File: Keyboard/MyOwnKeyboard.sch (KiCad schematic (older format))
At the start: 465 parts, among them J1 Mini-DIN-6, Q1 RFD14N05L, SW1 SW_SPST, SW10 SW_SPST, SW100 SW_SPST, SW101 SW_SPST, SW102 SW_SPST, SW103 SW_SPST, SW104 SW_SPST, SW105 SW_SPST, SW106 SW_SPST, SW107 SW_SPST, SW108 SW_SPST, SW109 SW_SPST, SW11 SW_SPST, SW110 SW_SPST, SW111 SW_SPST, SW112 SW_SPST, SW113 SW_SPST, SW114 SW_SPST, SW12 SW_SPST, SW13 SW_SPST, SW14 SW_SPST, SW15 SW_SPST, SW16 SW_SPST, SW17 SW_SPST, SW18 SW_SPST, SW19 SW_SPST, SW2 SW_SPST, SW20 SW_SPST, SW21 SW_SPST, SW22 SW_SPST, SW23 SW_SPST, SW24 SW_SPST, SW25 SW_SPST, SW26 SW_SPST, SW27 SW_SPST, SW28 SW_SPST, SW29 SW_SPST, SW3 SW_SPST, SW30 SW_SPST, SW31 SW_SPST, SW32 SW_SPST, SW33 SW_SPST, SW34 SW_SPST, SW35 SW_SPST, SW36 SW_SPST, SW37 SW_SPST, SW38 SW_SPST, SW39 SW_SPST, SW4 SW_SPST, SW40 SW_SPST, SW41 SW_SPST, SW42 SW_SPST, SW43 SW_SPST, SW44 SW_SPST, SW45 SW_SPST, SW46 SW_SPST, SW47 SW_SPST, SW48 SW_SPST, SW49 SW_SPST, SW5 SW_SPST, SW50 SW_SPST, SW51 SW_SPST, SW52 SW_SPST, SW53 SW_SPST, SW54 SW_SPST, SW55 SW_SPST, SW56 SW_SPST, SW57 SW_SPST, SW58 SW_SPST, SW59 SW_SPST, SW6 SW_SPST, SW60 SW_SPST, SW61 SW_SPST, SW62 SW_SPST, SW63 SW_SPST, SW64 SW_SPST, SW65 SW_SPST, SW66 SW_SPST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

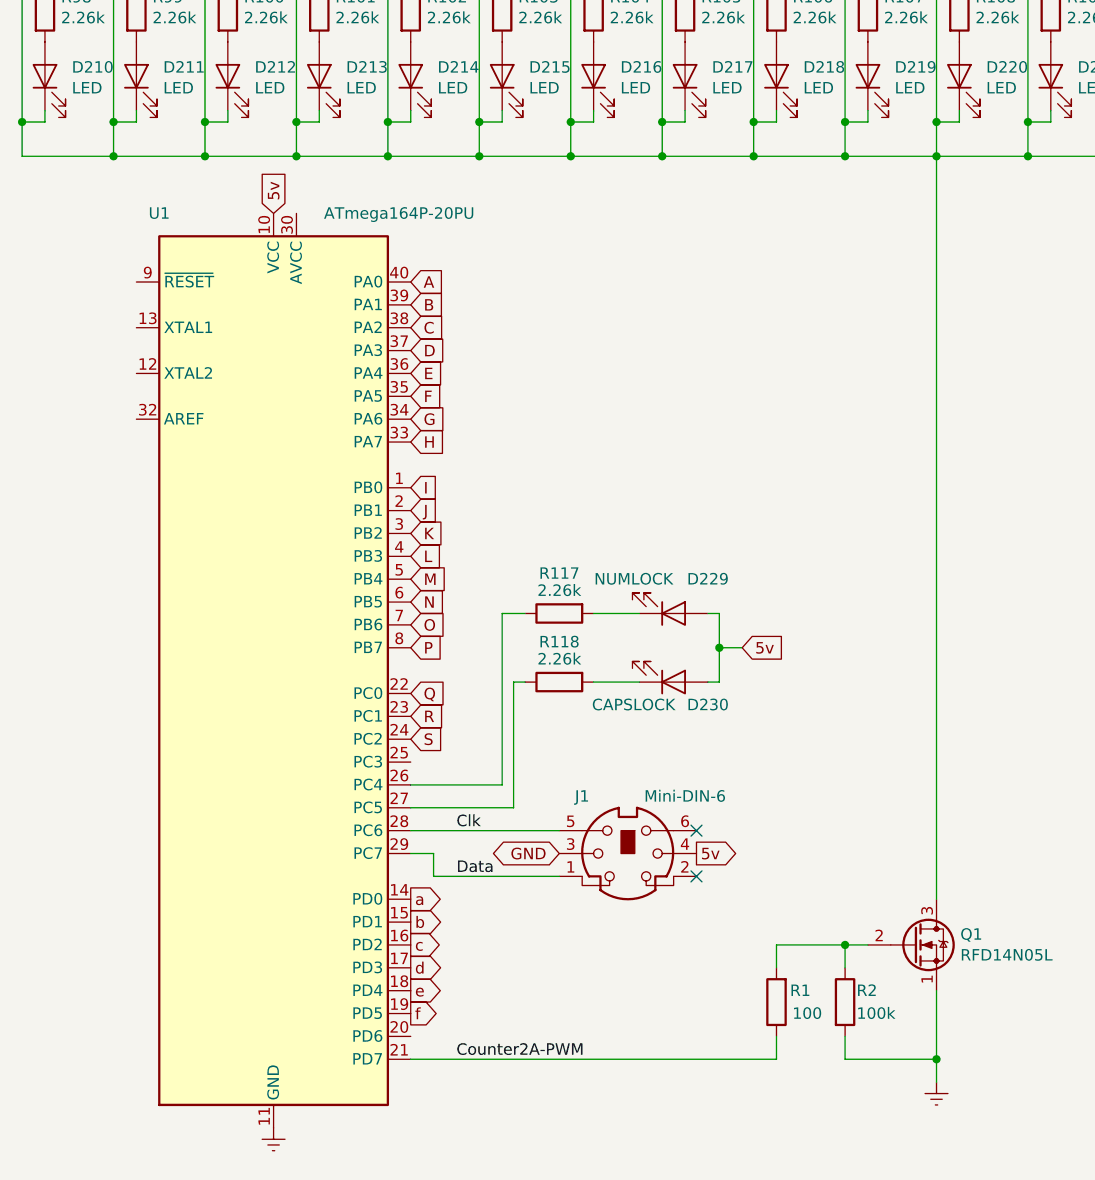
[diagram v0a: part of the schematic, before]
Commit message: Update keyboard to match changes to keypad
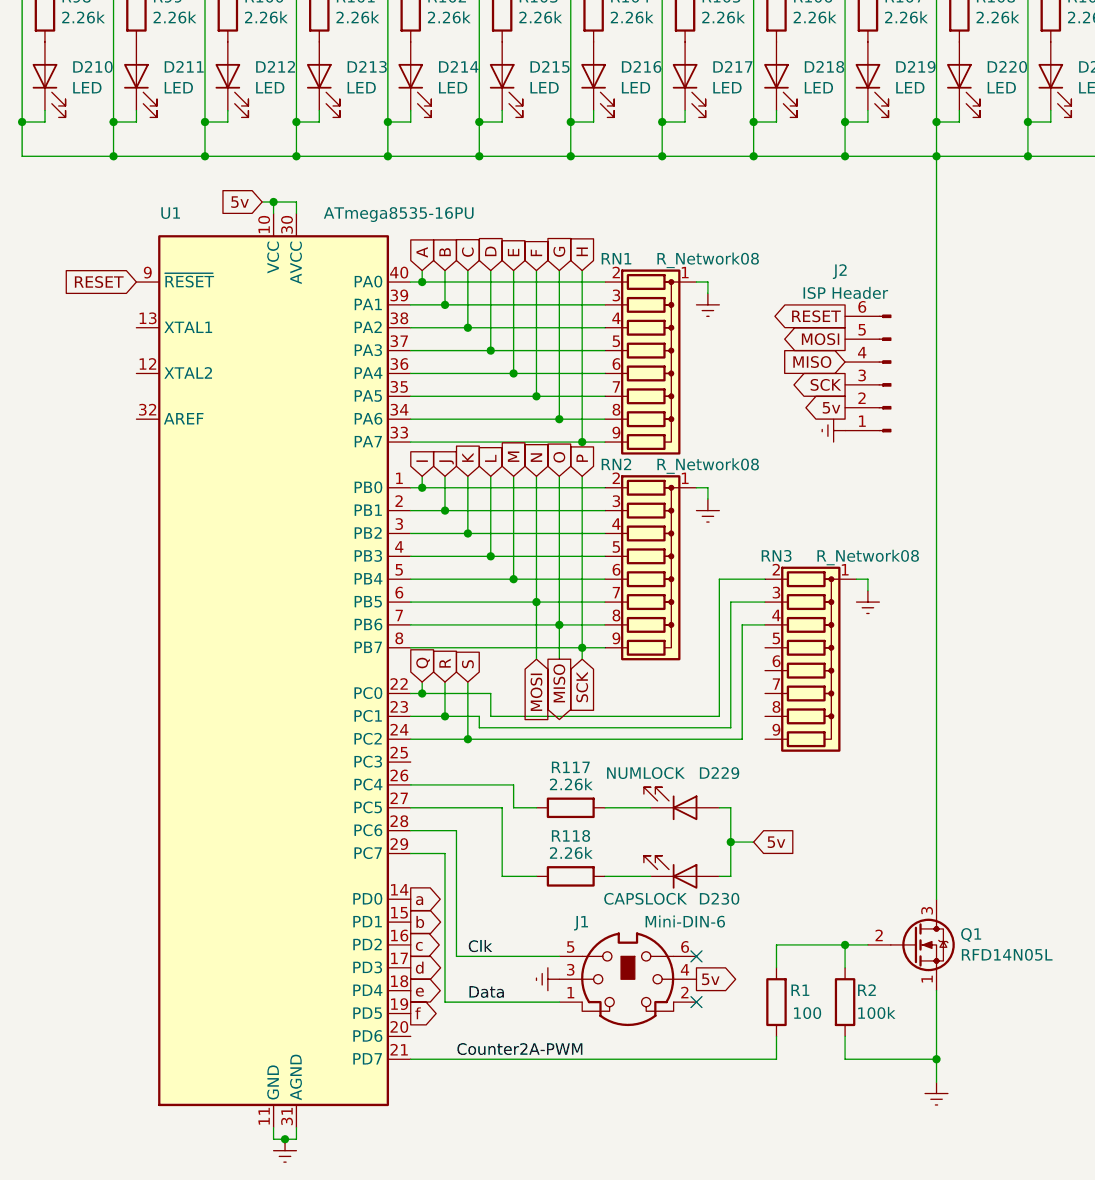
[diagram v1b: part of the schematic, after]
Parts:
- removed U1: ATmega164P-20PU, Package_DIP:DIP-40_W15.24mm, symbol MyOwnKeyboard-rescue:ATmega164P-20PU-MCU_Microchip_ATmega-MyOwnKeyboard-rescue
- added J2: ISP Header, Connector_PinHeader_2.54mm:PinHeader_2x03_P2.54mm_Vertical, symbol Connector:Conn_01x06_Male
- added RN1, RN2, RN3: R_Network08, Resistor_THT:R_Array_SIP9, symbol Device:R_Network08
- added U1: ATmega8535-16PU, Package_DIP:DIP-40_W15.24mm, symbol MCU_Microchip_ATmega:ATmega8535-16PU
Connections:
- net GND is gone; now on net Earth: J1.3
- net 5v: now also J2.2 (Pin_2), U1.10 (VCC), U1.30 (AVCC)
- net A: now also RN1.2 (R1), U1.40 (PA0)
- net B: now also RN1.3 (R2), U1.39 (PA1)
- net C: now also RN1.4 (R3), U1.38 (PA2)
- net Clk: now also U1.28 (PC6)
- net Counter2A-PWM: now also U1.21 (PD7)
- net D: now also RN1.5 (R4), U1.37 (PA3)
- net Data: now also U1.29 (PC7)
- net E: now also RN1.6 (R5), U1.36 (PA4)
- net Earth: now also J2.1 (Pin_1), RN1.1 (common), RN2.1 (common), RN3.1 (common), U1.11 (GND), U1.31 (AGND)
- net F: now also RN1.7 (R6), U1.35 (PA5)
- net G: now also RN1.8 (R7), U1.34 (PA6)
- net H: now also RN1.9 (R8), U1.33 (PA7)
- net I: now also RN2.2 (R1), U1.1 (PB0)
- net J: now also RN2.3 (R2), U1.2 (PB1)
- net K: now also RN2.4 (R3), U1.3 (PB2)
- net L: now also RN2.5 (R4), U1.4 (PB3)
- net M: now also RN2.6 (R5), U1.5 (PB4)
- net P: now also J2.3 (Pin_3), RN2.9 (R8), U1.8 (PB7)
- net Q: now also RN3.2 (R1), U1.22 (PC0)
- net R: now also RN3.3 (R2), U1.23 (PC1)
- net S: now also RN3.4 (R3), U1.24 (PC2)
- net a: now also U1.14 (PD0)
- net b: now also U1.15 (PD1)
- net c: now also U1.16 (PD2)
- net d: now also U1.17 (PD3)
- net e: now also U1.18 (PD4)
- net f: now also U1.19 (PD5)
- net at R117.1: now also U1.26 (PC4)
- net at R118.1: now also U1.27 (PC5)
- net N renamed MOSI
- net MOSI: now also J2.5 (Pin_5), RN2.7 (R6), U1.6 (PB5)
- net O renamed MISO
- net MISO: now also J2.4 (Pin_4), RN2.8 (R7), U1.7 (PB6)
- new net RESET: J2.6 (Pin_6), U1.9 (~RESET)
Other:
- moved on the sheet: D229, D230, J1, R117, R118

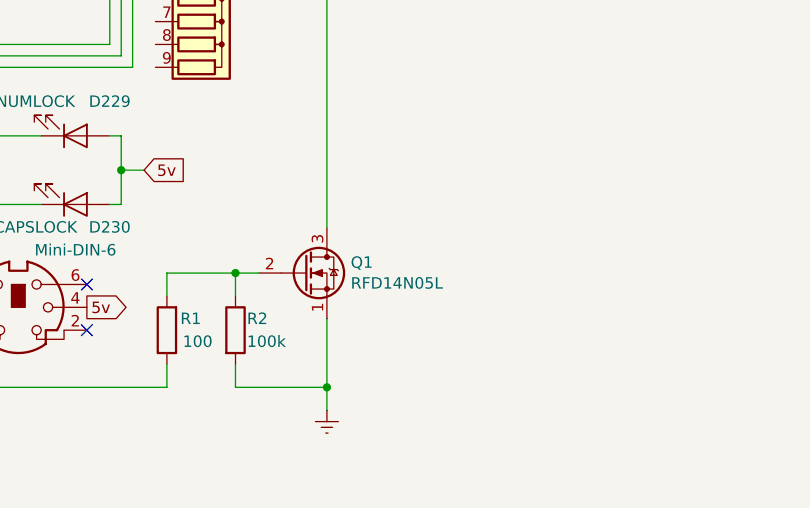
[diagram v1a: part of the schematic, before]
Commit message: Change PS/2 socket and transistor references
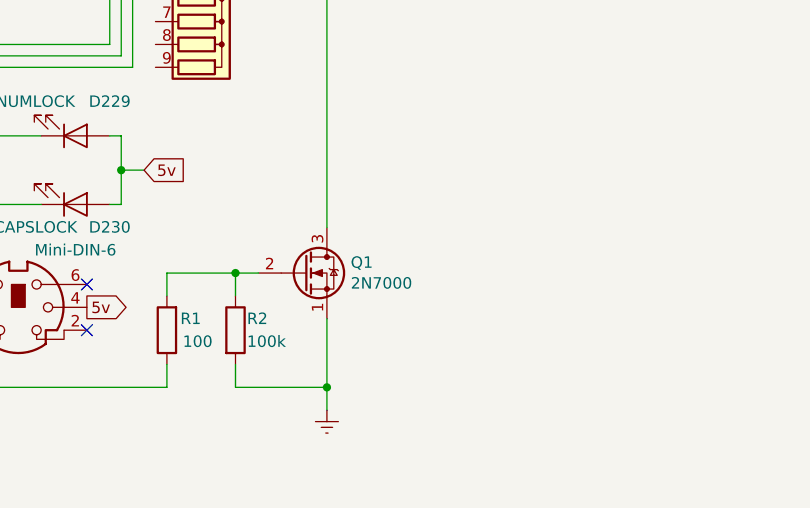
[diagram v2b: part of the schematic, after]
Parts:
- J1: footprint Connector_PinHeader_1.27mm:PinHeader_1x06_P1.27mm_Vertical -> MyOwnKeyboard:Connector_Mini-DIN_Female_6Pin_2rows
- Q1: value RFD14N05L -> 2N7000; footprint Package_TO_SOT_THT:TO-251-3-1EP_Horizontal_TabDown -> Package_TO_SOT_THT:TO-92_Inline
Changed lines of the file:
@@
 F 0 "J1" H 3450 15500 50  0000 C CNN
 F 1 "Mini-DIN-6" H 3000 15500 50  0000 C CNN
-F 2 "Connector_PinHeader_1.27mm:PinHeader_1x06_P1.27mm_Vertical" H 3250 15250 50  0001 C CNN
+F 2 "MyOwnKeyboard:Connector_Mini-DIN_Female_6Pin_2rows" H 3250 15250 50  0001 C CNN
 F 3 "http://service.powerdynamics.com/ec/Catalog17/Section%2011.pdf" H 3250 15250 50  0001 C CNN
 	1    3250 15250
@@
 P 4500 15100
 F 0 "Q1" H 4704 15146 50  0000 L CNN
-F 1 "RFD14N05L" H 4704 15055 50  0000 L CNN
-F 2 "Package_TO_SOT_THT:TO-251-3-1EP_Horizontal_TabDown" H 4700 15025 50  0001 L CIN
+F 1 "2N7000" H 4704 15055 50  0000 L CNN
+F 2 "Package_TO_SOT_THT:TO-92_Inline" H 4700 15025 50  0001 L CIN
 F 3 "https://www.fairchildsemi.com/datasheets/2N/2N7000.pdf" H 4500 15100 50  0001 L CNN
 	1    4500 15100

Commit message: Rename matrix driver pins
Nets are case-insensitive, so the driver pins are now 1-6 instead of a-f
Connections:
- net a renamed 1
- net b renamed 2
- net c renamed 3
- net d renamed 4
- net e renamed 5
- net f renamed 6
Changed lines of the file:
@@
 Text GLabel 2550 13950 1    50   Input ~ 0
 S
-Text GLabel 2300 14900 2    50   Output ~ 0
-a
 Text GLabel 2300 15000 2    50   Output ~ 0
-b
+2
 Text GLabel 2300 15100 2    50   Output ~ 0
-c
+3
 Text GLabel 2300 15200 2    50   Output ~ 0
-d
+4
 Text GLabel 2300 15300 2    50   Output ~ 0
-e
+5
 Text GLabel 2300 15400 2    50   Output ~ 0
-f
+6
 Text Label 2550 15150 0    50   ~ 0
 Clk
@@
 A
 Text GLabel 10000 5350 2    50   Input ~ 0
-f
+6
 Text GLabel 10000 4400 2    50   Input ~ 0
-e
+5
 Text GLabel 10000 3450 2    50   Input ~ 0
-d
+4
 Text GLabel 10000 2500 2    50   Input ~ 0
-c
+3
 Text GLabel 10000 1550 2    50   Input ~ 0
-b
+2
 Text GLabel 10000 600  2    50   Input ~ 0
-a
+1
 $Comp
 L Device:D D113
@@
 	-1   0    0    1
 $EndComp
+Text GLabel 2300 14900 2    50   Output ~ 0
+1
 $EndSCHEMATC

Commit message: Update diode and switch footprints
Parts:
- D1, D10, D100, D101, D102, D103, D104, D105, D106, D107, D108, D109, D11, D110, D111, D112, D113, D114, D12, D13, D14, D15, D16, D17, D18, D19, D2, D20, D21, D22, D23, D24, D25, D26, D27, D28, D29, D3, D30, D31, D32, D33, D34, D35, D36, D37, D38, D39, D4, D40, D41, D42, D43, D44, D45, D46, D47, D48, D49, D5, D50, D51, D52, D53, D54, D55, D56, D57, D58, D59, D6, D60, D61, D62, D63, D64, D65, D66, D67, D68, D69, D7, D70, D71, D72, D73, D74, D75, D76, D77, D78, D79, D8, D80, D81, D82, D83, D84, D85, D86, D87, D88, D89, D9, D90, D91, D92, D93, D94, D95, D96, D97, D98, D99: footprint Diode_THT:D_DO-35_SOD27_P7.62mm_Horizontal -> Diode_SMD:D_MiniMELF_Handsoldering
- SW1, SW10, SW100, SW101, SW102, SW103, SW104, SW105, SW106, SW107, SW108, SW109, SW11, SW110, SW111, SW112, SW113, SW114, SW12, SW13, SW14, SW15, SW16, SW17, SW18, SW19, SW2, SW20, SW21, SW22, SW23, SW24, SW25, SW26, SW27, SW28, SW29, SW3, SW30, SW31, SW32, SW33, SW34, SW35, SW36, SW37, SW38, SW39, SW4, SW40, SW41, SW42, SW43, SW44, SW45, SW46, SW47, SW48, SW49, SW5, SW50, SW51, SW52, SW53, SW54, SW55, SW56, SW57, SW58, SW59, SW6, SW60, SW61, SW62, SW63, SW64, SW65, SW66, SW67, SW68, SW69, SW7, SW70, SW71, SW72, SW73, SW74, SW75, SW76, SW77, SW78, SW79, SW8, SW80, SW81, SW82, SW83, SW84, SW85, SW86, SW87, SW88, SW89, SW9, SW90, SW91, SW92, SW93, SW94, SW95, SW96, SW97, SW98, SW99: footprint MyOwnKeyboard:RomerG -> MyOwnKeyboard:SW_Cherry_MX_1.00u_PCB

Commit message: Make matrix schematic compliant with pullup-sink method
See 64d5791
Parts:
- removed RN1, RN2, RN3: R_Network08, Resistor_THT:R_Array_SIP9, symbol Device:R_Network08
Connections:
- net A: now also D1.2 (A), D20.2 (A), D39.2 (A), D58.2 (A), D77.2 (A), D96.2 (A); no longer D1.1 (K), D20.1 (K), D39.1 (K), D58.1 (K), D77.1 (K), D96.1 (K)
- net B: now also D2.2 (A), D21.2 (A), D40.2 (A), D59.2 (A), D78.2 (A), D97.2 (A); no longer D2.1 (K), D21.1 (K), D40.1 (K), D59.1 (K), D78.1 (K), D97.1 (K)
- net C: now also D22.2 (A), D3.2 (A), D41.2 (A), D60.2 (A), D79.2 (A), D98.2 (A); no longer D22.1 (K), D3.1 (K), D41.1 (K), D60.1 (K), D79.1 (K), D98.1 (K)
- net D: now also D23.2 (A), D4.2 (A), D42.2 (A), D61.2 (A), D80.2 (A), D99.2 (A); no longer D23.1 (K), D4.1 (K), D42.1 (K), D61.1 (K), D80.1 (K), D99.1 (K)
- net E: now also D100.2 (A), D24.2 (A), D43.2 (A), D5.2 (A), D62.2 (A), D81.2 (A); no longer D100.1 (K), D24.1 (K), D43.1 (K), D5.1 (K), D62.1 (K), D81.1 (K)
- net F: now also D101.2 (A), D25.2 (A), D44.2 (A), D6.2 (A), D63.2 (A), D82.2 (A); no longer D101.1 (K), D25.1 (K), D44.1 (K), D6.1 (K), D63.1 (K), D82.1 (K)
- net G: now also D102.2 (A), D26.2 (A), D45.2 (A), D64.2 (A), D7.2 (A), D83.2 (A); no longer D102.1 (K), D26.1 (K), D45.1 (K), D64.1 (K), D7.1 (K), D83.1 (K)
- net H: now also D103.2 (A), D27.2 (A), D46.2 (A), D65.2 (A), D8.2 (A), D84.2 (A); no longer D103.1 (K), D27.1 (K), D46.1 (K), D65.1 (K), D8.1 (K), D84.1 (K)
- net I: now also D104.2 (A), D28.2 (A), D47.2 (A), D66.2 (A), D85.2 (A), D9.2 (A); no longer D104.1 (K), D28.1 (K), D47.1 (K), D66.1 (K), D85.1 (K), D9.1 (K)
- net J: now also D10.2 (A), D105.2 (A), D29.2 (A), D48.2 (A), D67.2 (A), D86.2 (A); no longer D10.1 (K), D105.1 (K), D29.1 (K), D48.1 (K), D67.1 (K), D86.1 (K)
- net K: now also D106.2 (A), D11.2 (A), D30.2 (A), D49.2 (A), D68.2 (A), D87.2 (A); no longer D106.1 (K), D11.1 (K), D30.1 (K), D49.1 (K), D68.1 (K), D87.1 (K)
- net L: now also D107.2 (A), D12.2 (A), D31.2 (A), D50.2 (A), D69.2 (A), D88.2 (A); no longer D107.1 (K), D12.1 (K), D31.1 (K), D50.1 (K), D69.1 (K), D88.1 (K)
- net M: now also D108.2 (A), D13.2 (A), D32.2 (A), D51.2 (A), D70.2 (A), D89.2 (A); no longer D108.1 (K), D13.1 (K), D32.1 (K), D51.1 (K), D70.1 (K), D89.1 (K)
- net MISO: now also D110.2 (A), D15.2 (A), D34.2 (A), D53.2 (A), D72.2 (A), D91.2 (A); no longer D110.1 (K), D15.1 (K), D34.1 (K), D53.1 (K), D72.1 (K), D91.1 (K)
- net MOSI: now also D109.2 (A), D14.2 (A), D33.2 (A), D52.2 (A), D71.2 (A), D90.2 (A); no longer D109.1 (K), D14.1 (K), D33.1 (K), D52.1 (K), D71.1 (K), D90.1 (K)
- net P: now also D111.2 (A), D16.2 (A), D35.2 (A), D54.2 (A), D73.2 (A), D92.2 (A); no longer D111.1 (K), D16.1 (K), D35.1 (K), D54.1 (K), D73.1 (K), D92.1 (K)
- net Q: now also D112.2 (A), D17.2 (A), D36.2 (A), D55.2 (A), D74.2 (A), D93.2 (A); no longer D112.1 (K), D17.1 (K), D36.1 (K), D55.1 (K), D74.1 (K), D93.1 (K)
- net R: now also D113.2 (A), D18.2 (A), D37.2 (A), D56.2 (A), D75.2 (A), D94.2 (A); no longer D113.1 (K), D18.1 (K), D37.1 (K), D56.1 (K), D75.1 (K), D94.1 (K)
- net S: now also D114.2 (A), D19.2 (A), D38.2 (A), D57.2 (A), D76.2 (A), D95.2 (A); no longer D114.1 (K), D19.1 (K), D38.1 (K), D57.1 (K), D76.1 (K), D95.1 (K)
- net at SW1.2 (B): now also D1.1 (K); no longer D1.2 (A)
- net at SW20.2 (B): now also D20.1 (K); no longer D20.2 (A)
- net at SW39.2 (B): now also D39.1 (K); no longer D39.2 (A)
- net at SW58.2 (B): now also D58.1 (K); no longer D58.2 (A)
- net at SW77.2 (B): now also D77.1 (K); no longer D77.2 (A)
- net at SW96.2 (B): now also D96.1 (K); no longer D96.2 (A)
- net at SW2.2 (B): now also D2.1 (K); no longer D2.2 (A)
- net at SW21.2 (B): now also D21.1 (K); no longer D21.2 (A)
- net at SW40.2 (B): now also D40.1 (K); no longer D40.2 (A)
- net at SW59.2 (B): now also D59.1 (K); no longer D59.2 (A)
- net at SW78.2 (B): now also D78.1 (K); no longer D78.2 (A)
- net at SW97.2 (B): now also D97.1 (K); no longer D97.2 (A)
- net at SW3.2 (B): now also D3.1 (K); no longer D3.2 (A)
- net at SW22.2 (B): now also D22.1 (K); no longer D22.2 (A)
- net at SW41.2 (B): now also D41.1 (K); no longer D41.2 (A)
- net at SW60.2 (B): now also D60.1 (K); no longer D60.2 (A)
- net at SW79.2 (B): now also D79.1 (K); no longer D79.2 (A)
- net at SW98.2 (B): now also D98.1 (K); no longer D98.2 (A)
- net at SW4.2 (B): now also D4.1 (K); no longer D4.2 (A)
- net at SW23.2 (B): now also D23.1 (K); no longer D23.2 (A)
- net at SW42.2 (B): now also D42.1 (K); no longer D42.2 (A)
- net at SW61.2 (B): now also D61.1 (K); no longer D61.2 (A)
- net at SW80.2 (B): now also D80.1 (K); no longer D80.2 (A)
- net at SW99.2 (B): now also D99.1 (K); no longer D99.2 (A)
- net at SW5.2 (B): now also D5.1 (K); no longer D5.2 (A)
- net at SW24.2 (B): now also D24.1 (K); no longer D24.2 (A)
- net at SW43.2 (B): now also D43.1 (K); no longer D43.2 (A)
- net at SW62.2 (B): now also D62.1 (K); no longer D62.2 (A)
- net at SW81.2 (B): now also D81.1 (K); no longer D81.2 (A)
- net at SW100.2 (B): now also D100.1 (K); no longer D100.2 (A)
- net at SW6.2 (B): now also D6.1 (K); no longer D6.2 (A)
- net at SW25.2 (B): now also D25.1 (K); no longer D25.2 (A)
- net at SW44.2 (B): now also D44.1 (K); no longer D44.2 (A)
- net at SW63.2 (B): now also D63.1 (K); no longer D63.2 (A)
- net at SW82.2 (B): now also D82.1 (K); no longer D82.2 (A)
- net at SW101.2 (B): now also D101.1 (K); no longer D101.2 (A)
- net at SW7.2 (B): now also D7.1 (K); no longer D7.2 (A)
- net at SW26.2 (B): now also D26.1 (K); no longer D26.2 (A)
- net at SW45.2 (B): now also D45.1 (K); no longer D45.2 (A)
- net at SW64.2 (B): now also D64.1 (K); no longer D64.2 (A)
- net at SW83.2 (B): now also D83.1 (K); no longer D83.2 (A)
- net at SW102.2 (B): now also D102.1 (K); no longer D102.2 (A)
- net at SW8.2 (B): now also D8.1 (K); no longer D8.2 (A)
- net at SW27.2 (B): now also D27.1 (K); no longer D27.2 (A)
- net at SW46.2 (B): now also D46.1 (K); no longer D46.2 (A)
- net at SW65.2 (B): now also D65.1 (K); no longer D65.2 (A)
- net at SW84.2 (B): now also D84.1 (K); no longer D84.2 (A)
- net at SW103.2 (B): now also D103.1 (K); no longer D103.2 (A)
- net at SW9.2 (B): now also D9.1 (K); no longer D9.2 (A)
- net at SW28.2 (B): now also D28.1 (K); no longer D28.2 (A)
- net at SW47.2 (B): now also D47.1 (K); no longer D47.2 (A)
- net at SW66.2 (B): now also D66.1 (K); no longer D66.2 (A)
- net at SW85.2 (B): now also D85.1 (K); no longer D85.2 (A)
- net at SW104.2 (B): now also D104.1 (K); no longer D104.2 (A)
- net at SW10.2 (B): now also D10.1 (K); no longer D10.2 (A)
- net at SW29.2 (B): now also D29.1 (K); no longer D29.2 (A)
- net at SW48.2 (B): now also D48.1 (K); no longer D48.2 (A)
- net at SW67.2 (B): now also D67.1 (K); no longer D67.2 (A)
- net at SW86.2 (B): now also D86.1 (K); no longer D86.2 (A)
- net at SW105.2 (B): now also D105.1 (K); no longer D105.2 (A)
- net at SW11.2 (B): now also D11.1 (K); no longer D11.2 (A)
- net at SW30.2 (B): now also D30.1 (K); no longer D30.2 (A)
- net at SW49.2 (B): now also D49.1 (K); no longer D49.2 (A)
- net at SW68.2 (B): now also D68.1 (K); no longer D68.2 (A)
- net at SW87.2 (B): now also D87.1 (K); no longer D87.2 (A)
- net at SW106.2 (B): now also D106.1 (K); no longer D106.2 (A)
- net at SW12.2 (B): now also D12.1 (K); no longer D12.2 (A)
- net at SW31.2 (B): now also D31.1 (K); no longer D31.2 (A)
- net at SW50.2 (B): now also D50.1 (K); no longer D50.2 (A)
- net at SW69.2 (B): now also D69.1 (K); no longer D69.2 (A)
- net at SW88.2 (B): now also D88.1 (K); no longer D88.2 (A)
- net at SW107.2 (B): now also D107.1 (K); no longer D107.2 (A)
- net at SW13.2 (B): now also D13.1 (K); no longer D13.2 (A)
- net at SW32.2 (B): now also D32.1 (K); no longer D32.2 (A)
- net at SW51.2 (B): now also D51.1 (K); no longer D51.2 (A)
- net at SW70.2 (B): now also D70.1 (K); no longer D70.2 (A)
- net at SW89.2 (B): now also D89.1 (K); no longer D89.2 (A)
- net at SW108.2 (B): now also D108.1 (K); no longer D108.2 (A)
- net at SW14.2 (B): now also D14.1 (K); no longer D14.2 (A)
- net at SW33.2 (B): now also D33.1 (K); no longer D33.2 (A)
- net at SW52.2 (B): now also D52.1 (K); no longer D52.2 (A)
- net at SW71.2 (B): now also D71.1 (K); no longer D71.2 (A)
- net at SW90.2 (B): now also D90.1 (K); no longer D90.2 (A)
- net at SW109.2 (B): now also D109.1 (K); no longer D109.2 (A)
- net at SW15.2 (B): now also D15.1 (K); no longer D15.2 (A)
- net at SW34.2 (B): now also D34.1 (K); no longer D34.2 (A)
- net at SW53.2 (B): now also D53.1 (K); no longer D53.2 (A)
- net at SW72.2 (B): now also D72.1 (K); no longer D72.2 (A)
- net at SW91.2 (B): now also D91.1 (K); no longer D91.2 (A)
- net at SW110.2 (B): now also D110.1 (K); no longer D110.2 (A)
- net at SW16.2 (B): now also D16.1 (K); no longer D16.2 (A)
- net at SW35.2 (B): now also D35.1 (K); no longer D35.2 (A)
- net at SW54.2 (B): now also D54.1 (K); no longer D54.2 (A)
- net at SW73.2 (B): now also D73.1 (K); no longer D73.2 (A)
- net at SW92.2 (B): now also D92.1 (K); no longer D92.2 (A)
- net at SW111.2 (B): now also D111.1 (K); no longer D111.2 (A)
- net at SW17.2 (B): now also D17.1 (K); no longer D17.2 (A)
- net at SW36.2 (B): now also D36.1 (K); no longer D36.2 (A)
- net at SW55.2 (B): now also D55.1 (K); no longer D55.2 (A)
- net at SW74.2 (B): now also D74.1 (K); no longer D74.2 (A)
- net at SW93.2 (B): now also D93.1 (K); no longer D93.2 (A)
- net at SW112.2 (B): now also D112.1 (K); no longer D112.2 (A)
- net at SW18.2 (B): now also D18.1 (K); no longer D18.2 (A)
- net at SW37.2 (B): now also D37.1 (K); no longer D37.2 (A)
- net at SW56.2 (B): now also D56.1 (K); no longer D56.2 (A)
- net at SW75.2 (B): now also D75.1 (K); no longer D75.2 (A)
- net at SW94.2 (B): now also D94.1 (K); no longer D94.2 (A)
- net at SW113.2 (B): now also D113.1 (K); no longer D113.2 (A)
- net at SW19.2 (B): now also D19.1 (K); no longer D19.2 (A)
- net at SW38.2 (B): now also D38.1 (K); no longer D38.2 (A)
- net at SW57.2 (B): now also D57.1 (K); no longer D57.2 (A)
- net at SW76.2 (B): now also D76.1 (K); no longer D76.2 (A)
- net at SW95.2 (B): now also D95.1 (K); no longer D95.2 (A)
- net at SW114.2 (B): now also D114.1 (K); no longer D114.2 (A)
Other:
- moved on the sheet: J2

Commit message: Reverse diode orientation and reduce pad size
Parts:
- D1, D10, D100, D101, D102, D103, D104, D105, D106, D107, D108, D109, D11, D110, D111, D112, D113, D114, D12, D13, D14, D15, D16, D17, D18, D19, D2, D20, D21, D22, D23, D24, D25, D26, D27, D28, D29, D3, D30, D31, D32, D33, D34, D35, D36, D37, D38, D39, D4, D40, D41, D42, D43, D44, D45, D46, D47, D48, D49, D5, D50, D51, D52, D53, D54, D55, D56, D57, D58, D59, D6, D60, D61, D62, D63, D64, D65, D66, D67, D68, D69, D7, D70, D71, D72, D73, D74, D75, D76, D77, D78, D79, D8, D80, D81, D82, D83, D84, D85, D86, D87, D88, D89, D9, D90, D91, D92, D93, D94, D95, D96, D97, D98, D99: footprint Diode_SMD:D_MiniMELF_Handsoldering -> Diode_SMD:D_MiniMELF

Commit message: Add component metadata incl. KiCost part details
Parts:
- D1, D10, D100, D101, D102, D103, D104, D105, D106, D107, D108, D109, D11, D110, D111, D112, D113, D114, D12, D13, D14, D15, D16, D17, D18, D19, D2, D20, D21, D22, D23, D24, D25, D26, D27, D28, D29, D3, D30, D31, D32, D33, D34, D35, D36, D37, D38, D39, D4, D40, D41, D42, D43, D44, D45, D46, D47, D48, D49, D5, D50, D51, D52, D53, D54, D55, D56, D57, D58, D59, D6, D60, D61, D62, D63, D64, D65, D66, D67, D68, D69, D7, D70, D71, D72, D73, D74, D75, D76, D77, D78, D79, D8, D80, D81, D82, D83, D84, D85, D86, D87, D88, D89, D9, D90, D91, D92, D93, D94, D95, D96, D97, D98, D99: kicost:AliExpress:link (none) -> https://www.aliexpress.com/item/4000331505052.html; kicost:AliExpress:pricing (none) -> 1:AUD0.0247; manf# (none) -> LL4148
- D115, D116, D117, D118, D119, D120, D121, D122, D123, D124, D125, D126, D127, D128, D129, D130, D131, D132, D133, D134, D135, D136, D137, D138, D139, D140, D141, D142, D143, D144, D145, D146, D147, D148, D149, D150, D151, D152, D153, D154, D155, D156, D157, D158, D159, D160, D161, D162, D163, D164, D165, D166, D167, D168, D169, D170, D171, D172, D173, D174, D175, D176, D177, D178, D179, D180, D181, D182, D183, D184, D185, D186, D187, D188, D189, D190, D191, D192, D193, D194, D195, D196, D197, D198, D199, D200, D201, D202, D203, D204, D205, D206, D207, D208, D209, D210, D211, D212, D213, D214, D215, D216, D217, D218, D219, D220, D221, D222, D223, D224, D225, D226, D227, D228, D229, D230: manf# (none) -> 158301250
- J1: kicost:AliExpress:link (none) -> https://www.aliexpress.com/item/32878704114.html; kicost:AliExpress:pricing (none) -> 1:AUD0.554
- J2: manf# (none) -> 67996-406HLF
- Q1: manf# (none) -> 2N7000
- R1: kicost:AliExpress:link (none) -> https://www.aliexpress.com/item/32868987725.html; kicost:AliExpress:pricing (none) -> 1:AUD0.01; manf# (none) -> 2446869
- R10, R100, R101, R102, R103, R104, R105, R106, R107, R108, R109, R11, R110, R111, R112, R113, R114, R115, R116, R117, R118, R12, R13, R14, R15, R16, R17, R18, R19, R20, R21, R22, R23, R24, R25, R26, R27, R28, R29, R3, R30, R31, R32, R33, R34, R35, R36, R37, R38, R39, R4, R40, R41, R42, R43, R44, R45, R46, R47, R48, R49, R5, R50, R51, R52, R53, R54, R55, R56, R57, R58, R59, R6, R60, R61, R62, R63, R64, R65, R66, R67, R68, R69, R7, R70, R71, R72, R73, R74, R75, R76, R77, R78, R79, R8, R80, R81, R82, R83, R84, R85, R86, R87, R88, R89, R9, R90, R91, R92, R93, R94, R95, R96, R97, R98, R99: kicost:AliExpress:link (none) -> https://www.aliexpress.com/item/32868991875.html; kicost:AliExpress:pricing (none) -> 1:AUD0.0146; manf# (none) -> 2446941
- R2: kicost:AliExpress:link (none) -> https://www.aliexpress.com/item/32868987725.html; kicost:AliExpress:pricing (none) -> 1:AUD0.01; manf# (none) -> 2446868
- SW1, SW10, SW100, SW101, SW102, SW103, SW104, SW105, SW106, SW107, SW108, SW109, SW11, SW110, SW111, SW112, SW113, SW114, SW12, SW13, SW14, SW15, SW16, SW17, SW18, SW19, SW2, SW20, SW21, SW22, SW23, SW24, SW25, SW26, SW27, SW28, SW29, SW3, SW30, SW31, SW32, SW33, SW34, SW35, SW36, SW37, SW38, SW39, SW4, SW40, SW41, SW42, SW43, SW44, SW45, SW46, SW47, SW48, SW49, SW5, SW50, SW51, SW52, SW53, SW54, SW55, SW56, SW57, SW58, SW59, SW6, SW60, SW61, SW62, SW63, SW64, SW65, SW66, SW67, SW68, SW69, SW7, SW70, SW71, SW72, SW73, SW74, SW75, SW76, SW77, SW78, SW79, SW8, SW80, SW81, SW82, SW83, SW84, SW85, SW86, SW87, SW88, SW89, SW9, SW90, SW91, SW92, SW93, SW94, SW95, SW96, SW97, SW98, SW99: kicost:AliExpress:link (none) -> https://www.aliexpress.com/item/4001252892240.html; kicost:AliExpress:pricing (none) -> 1:AUD0.529
- U1: manf# (none) -> ATmega8535-16PU
